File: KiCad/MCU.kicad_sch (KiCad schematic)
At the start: 40 parts, among them J3 Conn_01x10_Pin, J4 Conn_01x10_Pin, J5 Conn_01x10_Pin, J6 Conn_01x10_Pin, J7 Conn_01x10_Pin, Q1 2N7002, Q2 2N7002, SW1 SW_Push, SW2 SW_Push, SW3 SW_Push, U5 STM32L476RGT6, U6 CP2102N-Axx-xQFN24, Y1 Crystal_GND24

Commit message: changed components and excluded from BOM
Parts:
- J3, J4, J5, J6, J7: now left out of the parts list
- R12: JLCPCB Part C65831 -> C23171
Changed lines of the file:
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@@
 		(body_style 1)
 		(exclude_from_sim no)
-		(in_bom yes)
+		(in_bom no)
 		(on_board yes)
 		(in_pos_files yes)
@@
 		(body_style 1)
 		(exclude_from_sim no)
-		(in_bom yes)
+		(in_bom no)
 		(on_board yes)
 		(in_pos_files yes)
@@
 		(body_style 1)
 		(exclude_from_sim no)
-		(in_bom yes)
+		(in_bom no)
 		(on_board yes)
 		(in_pos_files yes)
@@
 		(body_style 1)
 		(exclude_from_sim no)
-		(in_bom yes)
+		(in_bom no)
 		(on_board yes)
 		(in_pos_files yes)
@@
 			)
 		)
-		(property "JLCPCB Part" "C65831"
+		(property "JLCPCB Part" "C23171"
 			(at 101.6 48.26 90)
 			(hide yes)
@@
 		(body_style 1)
 		(exclude_from_sim no)
-		(in_bom yes)
+		(in_bom no)
 		(on_board yes)
 		(in_pos_files yes)

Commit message: changed more part#
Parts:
- C13, C14, C15, C16, C17: JLCPCB Part C1590 -> C1591
- Q1, Q2: JLCPCB Part C8545 -> C916396
- R11, R13, R14, R16, R20, R21: JLCPCB Part C25804 -> C2930027
- R12: JLCPCB Part C23171 -> C234529
- R15: JLCPCB Part C22809 -> C114682
- R17, R19, R24: JLCPCB Part C21190 -> C2907002
- R18: JLCPCB Part C22775 -> C122970
- R23: JLCPCB Part C25819 -> C2907042
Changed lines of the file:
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@@
 			)
 		)
-		(property "JLCPCB Part" "C1590"
+		(property "JLCPCB Part" "C1591"
 			(at 113.03 31.75 0)
 			(hide yes)
@@
 			)
 		)
-		(property "JLCPCB Part" "C8545"
+		(property "JLCPCB Part" "C916396"
 			(at 138.43 81.28 0)
 			(hide yes)
@@
 			)
 		)
-		(property "JLCPCB Part" "C21190"
+		(property "JLCPCB Part" "C2907002"
 			(at 129.54 81.28 90)
 			(hide yes)
@@
 			)
 		)
-		(property "JLCPCB Part" "C1590"
+		(property "JLCPCB Part" "C1591"
 			(at 99.06 31.75 0)
 			(hide yes)
@@
 			)
 		)
-		(property "JLCPCB Part" "C22809"
+		(property "JLCPCB Part" "C114682"
 			(at 135.89 121.92 0)
 			(hide yes)
@@
 			)
 		)
-		(property "JLCPCB Part" "C25804"
+		(property "JLCPCB Part" "C2930027"
 			(at 106.68 76.2 90)
 			(hide yes)
@@
 			)
 		)
-		(property "JLCPCB Part" "C21190"
+		(property "JLCPCB Part" "C2907002"
 			(at 208.28 46.99 0)
 			(hide yes)
@@
 			)
 		)
-		(property "JLCPCB Part" "C25804"
+		(property "JLCPCB Part" "C2930027"
 			(at 102.87 101.6 0)
 			(hide yes)
@@
 			)
 		)
-		(property "JLCPCB Part" "C1590"
+		(property "JLCPCB Part" "C1591"
 			(at 127 31.75 0)
 			(hide yes)
@@
 			)
 		)
-		(property "JLCPCB Part" "C25804"
+		(property "JLCPCB Part" "C2930027"
 			(at 129.54 115.57 90)
 			(hide yes)
@@
 			)
 		)
-		(property "JLCPCB Part" "C8545"
+		(property "JLCPCB Part" "C916396"
 			(at 33.02 175.26 0)
 			(hide yes)
@@
 			)
 		)
-		(property "JLCPCB Part" "C25804"
+		(property "JLCPCB Part" "C2930027"
 			(at 130.81 53.34 90)
 			(hide yes)
@@
 			)
 		)
-		(property "JLCPCB Part" "C1590"
+		(property "JLCPCB Part" "C1591"
 			(at 71.12 163.83 0)
 			(hide yes)
@@
 			)
 		)
-		(property "JLCPCB Part" "C22775"
+		(property "JLCPCB Part" "C122970"
 			(at 50.8 177.8 90)
 			(hide yes)
@@
 			)
 		)
-		(property "JLCPCB Part" "C25819"
+		(property "JLCPCB Part" "C2907042"
 			(at 177.8 59.69 0)
 			(hide yes)
@@
 			)
 		)
-		(property "JLCPCB Part" "C25804"
+		(property "JLCPCB Part" "C2930027"
 			(at 22.86 168.91 90)
 			(hide yes)
@@
 			)
 		)
-		(property "JLCPCB Part" "C23171"
+		(property "JLCPCB Part" "C234529"
 			(at 101.6 48.26 90)
 			(hide yes)
@@
 			)
 		)
-		(property "JLCPCB Part" "C21190"
+		(property "JLCPCB Part" "C2907002"
 			(at 43.18 167.64 90)
 			(hide yes)
@@
 			)
 		)
-		(property "JLCPCB Part" "C1590"
+		(property "JLCPCB Part" "C1591"
 			(at 139.7 31.75 0)
 			(hide yes)
@@
 			)
 		)
-		(property "JLCPCB Part" "C25804"
+		(property "JLCPCB Part" "C2930027"
 			(at 93.98 101.6 0)
 			(hide yes)

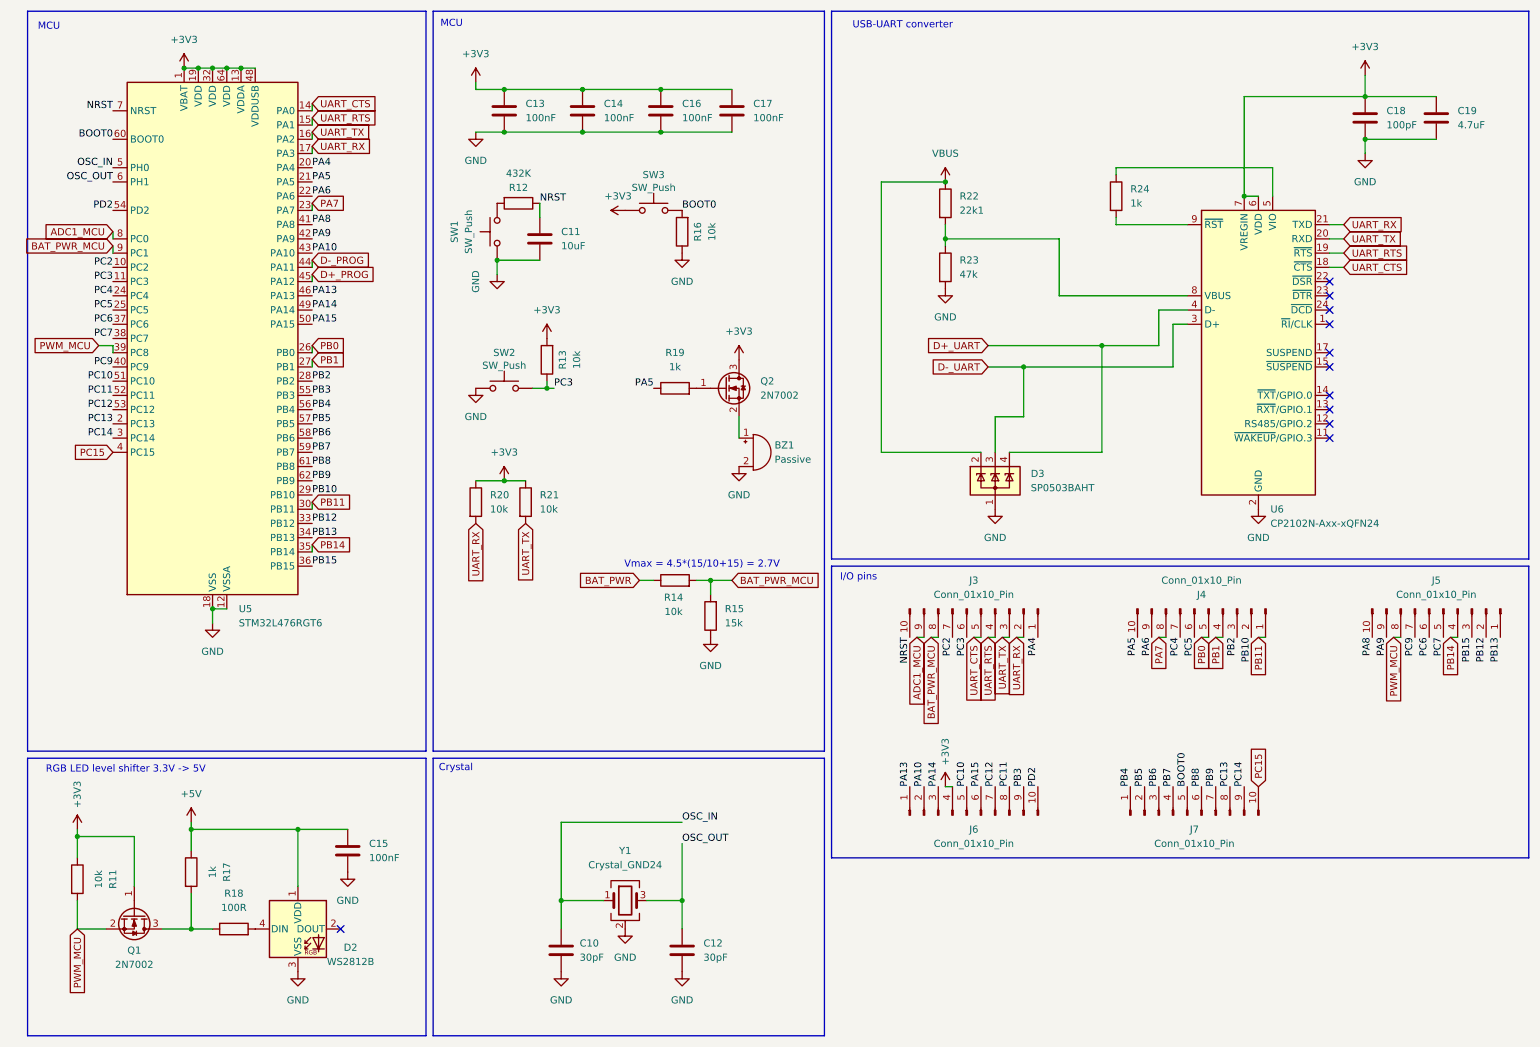
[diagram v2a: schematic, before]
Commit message: changed some out of stock parts
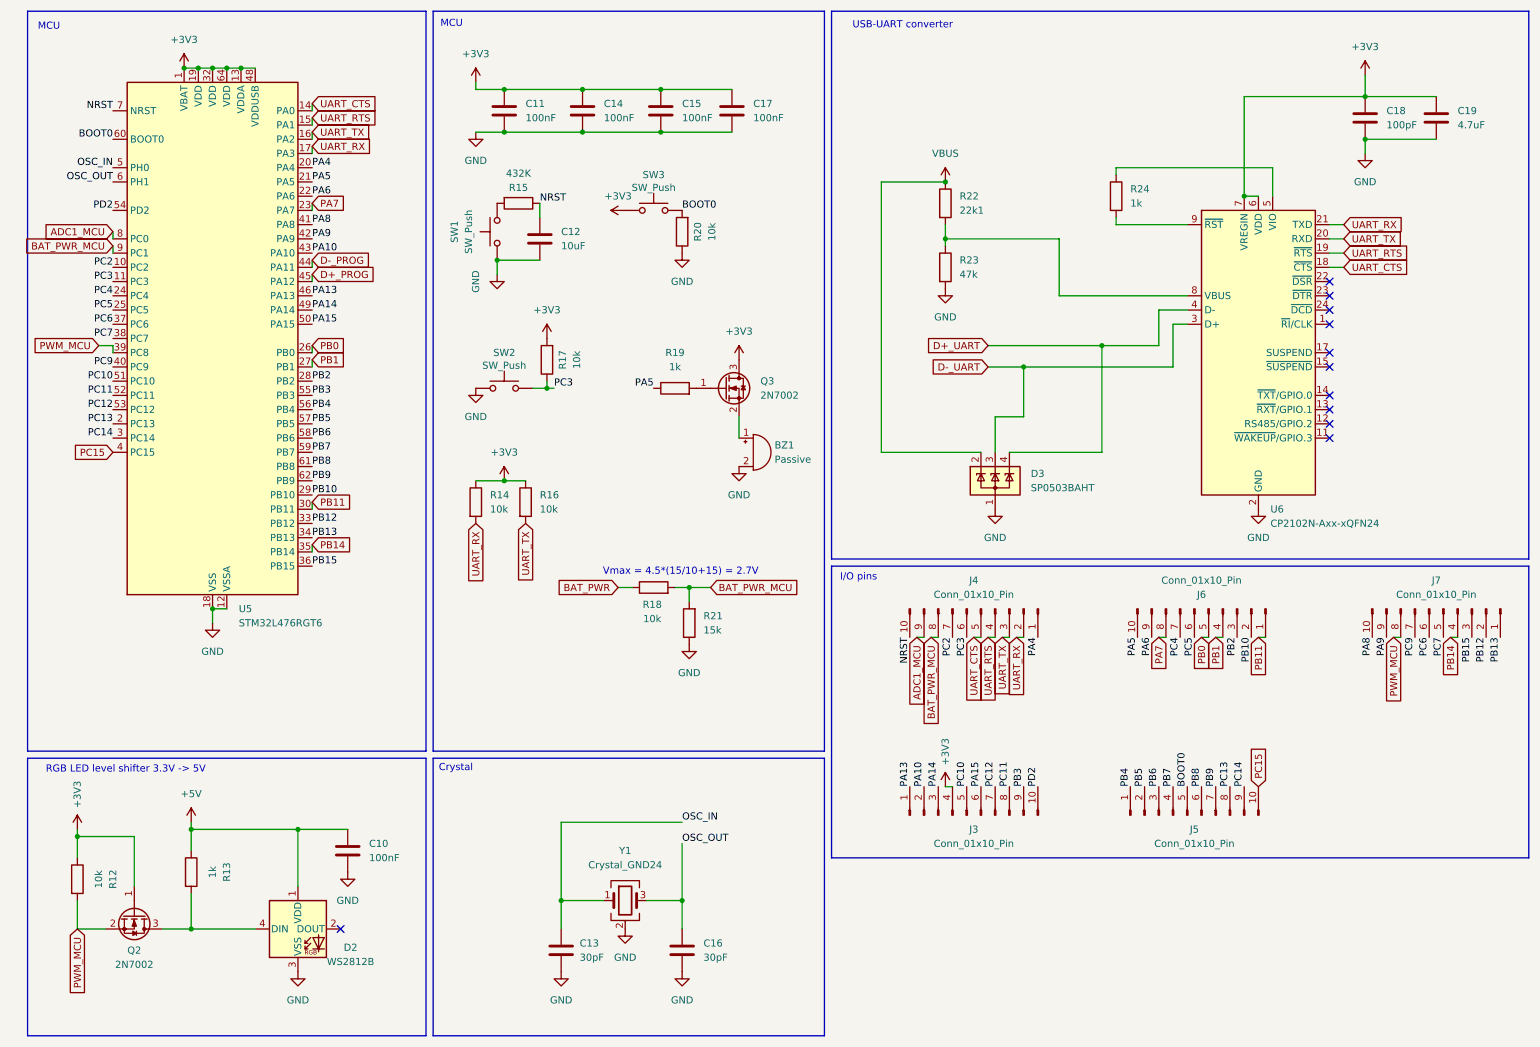
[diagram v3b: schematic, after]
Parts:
- removed R18: 100R, Resistor_SMD:R_0603_1608Metric_Pad0.98x0.95mm_HandSolder, symbol Device:R
- J3: renamed from J6; JLCPCB Part (none) -> C42431818; now in the parts list
- J4: renamed from J3; JLCPCB Part (none) -> C42431818; now in the parts list
- J5: renamed from J7; JLCPCB Part (none) -> C42431818; now in the parts list
- J6: renamed from J4; JLCPCB Part (none) -> C42431818; now in the parts list
- J7: renamed from J5; JLCPCB Part (none) -> C42431818; now in the parts list
- renumbered C15 to C10, C13 to C11, C11 to C12, C10 to C13, C16 to C15, C12 to C16, Q1 to Q2, Q2 to Q3, R11 to R12, R17 to R13, R20 to R14, R12 to R15, R21 to R16, R13 to R17, R14 to R18, R16 to R20, R15 to R21
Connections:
- net at D2.4 (DIN): now also Q2.3 (D), R13.2
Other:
- moved on the sheet: R18, R21
